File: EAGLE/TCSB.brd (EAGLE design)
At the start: 160 x 100 mm, 0 parts

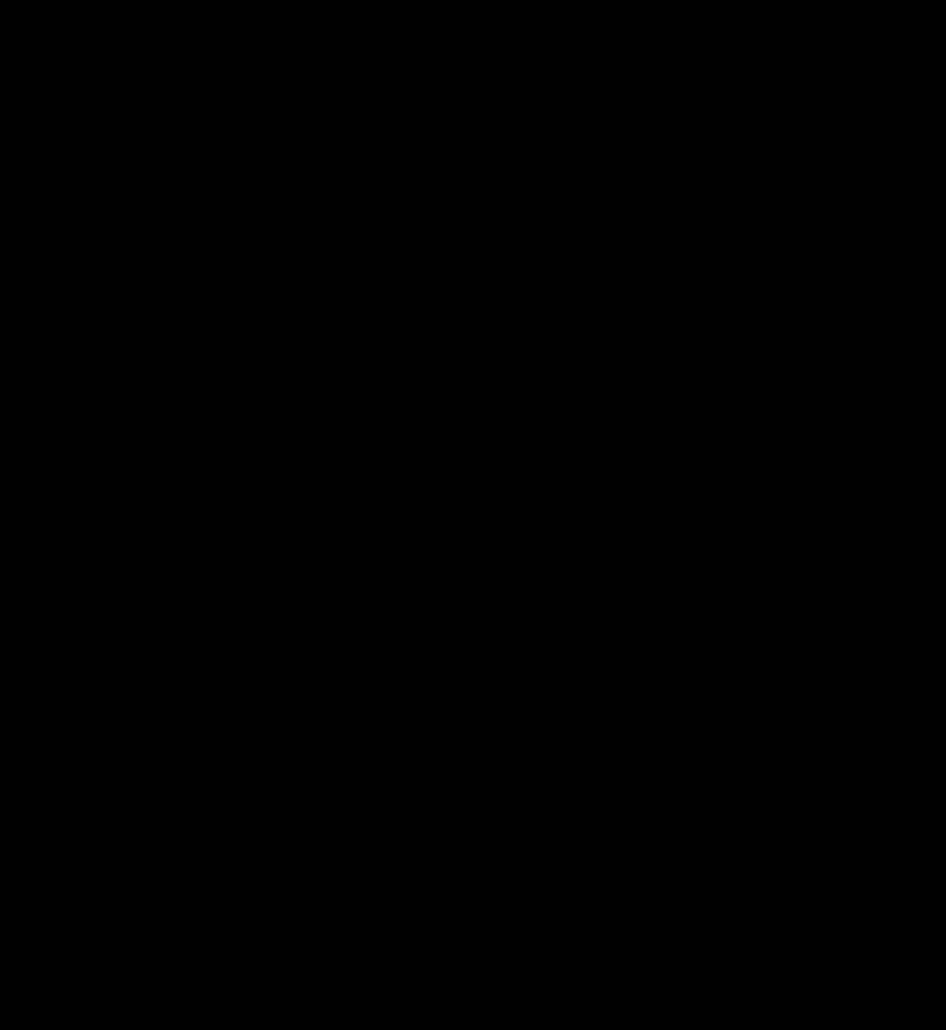
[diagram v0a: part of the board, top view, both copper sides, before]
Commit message: added board and firmware for two versions
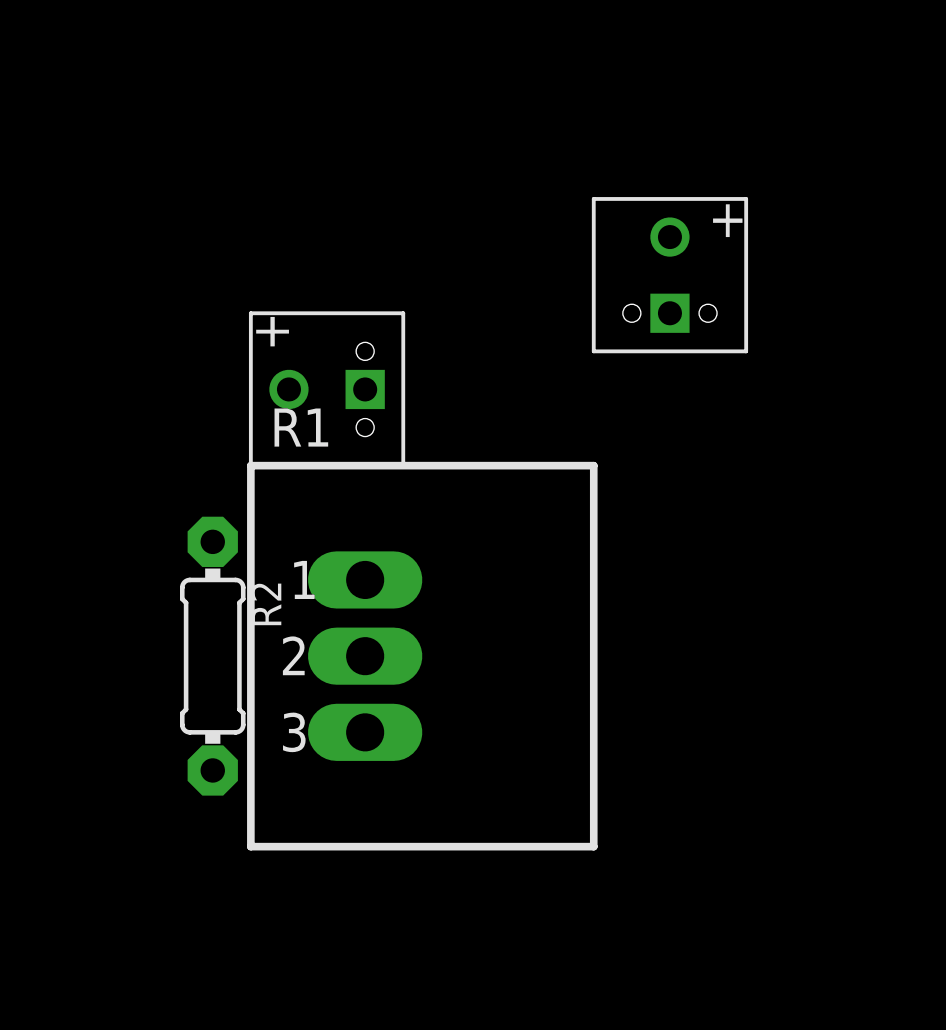
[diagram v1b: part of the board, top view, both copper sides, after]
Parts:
- added R1: (no value), bourns:308
- added R2: 10ohms, adafruit:0204/7
- added U$1, U$2: RCA-YELLOW, con-rca:RCA-YELLOW
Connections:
- new net N$1: R2.2, U$2.P$1
- new net N$2: R1.2, U$1.P$2, U$2.P$2
- new net N$3: R1.3, U$1.P$1
- new net N$4: R1.1, R2.1
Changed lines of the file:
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@@
 <layer number="48" name="Document" color="7" fill="1" visible="yes" active="yes"/>
 <layer number="49" name="Reference" color="7" fill="1" visible="yes" active="yes"/>
+<layer number="50" name="dxf" color="7" fill="1" visible="no" active="yes"/>
 <layer number="51" name="tDocu" color="7" fill="1" visible="yes" active="yes"/>
 <layer number="52" name="bDocu" color="7" fill="1" visible="yes" active="yes"/>
+<layer number="53" name="tGND_GNDA" color="7" fill="9" visible="no" active="no"/>
+<layer number="54" name="bGND_GNDA" color="1" fill="9" visible="no" active="no"/>
+<layer number="56" name="wert" color="7" fill="1" visible="yes" active="yes"/>
 <layer number="90" name="Modules" color="5" fill="1" visible="no" active="no"/>
 <layer number="91" name="Nets" color="2" fill="1" visible="no" active="no"/>
@@
 <layer number="97" name="Info" color="7" fill="1" visible="no" active="no"/>
 <layer number="98" name="Guide" color="6" fill="1" visible="no" active="no"/>
+<layer number="100" name="Muster" color="7" fill="1" visible="no" active="no"/>
+<layer number="101" name="Patch_Top" color="12" fill="4" visible="yes" active="yes"/>
+<layer number="102" name="Vscore" color="7" fill="1" visible="yes" active="yes"/>
+<layer number="104" name="Name" color="7" fill="1" visible="yes" active="yes"/>
+<layer number="116" name="Patch_BOT" color="9" fill="4" visible="yes" active="yes"/>
+<layer number="121" name="_tsilk" color="7" fill="1" visible="yes" active="yes"/>
+<layer number="122" name="_bsilk" color="7" fill="1" visible="yes" active="yes"/>
+<layer number="151" name="HeatSink" color="7" fill="1" visible="yes" active="yes"/>
+<layer number="200" name="200bmp" color="1" fill="10" visible="no" active="no"/>
+<layer number="201" name="201bmp" color="2" fill="1" visible="no" active="no"/>
+<layer number="202" name="202bmp" color="3" fill="1" visible="no" active="no"/>
+<layer number="203" name="203bmp" color="4" fill="10" visible="yes" active="yes"/>
+<layer number="204" name="204bmp" color="5" fill="10" visible="yes" active="yes"/>
+<layer number="205" name="205bmp" color="6" fill="10" visible="yes" active="yes"/>
+<layer number="206" name="206bmp" color="7" fill="10" visible="yes" active="yes"/>
+<layer number="207" name="207bmp" color="8" fill="10" visible="yes" active="yes"/>
+<layer number="208" name="208bmp" color="9" fill="10" visible="yes" active="yes"/>
+<layer number="250" name="Descript" color="7" fill="1" visible="no" active="no"/>
+<layer number="251" name="SMDround" color="7" fill="1" visible="no" active="no"/>
+<layer number="254" name="cooling" color="7" fill="1" visible="yes" active="yes"/>
 </layers>
 <board>
@@
 </autorouter>
 <elements>
+<element name="U$1" library="con-rca" package="RCA-YELLOW" value="RCA-YELLOW" x="33.02" y="25.4"/>
+<element name="U$2" library="con-rca" package="RCA-YELLOW" value="RCA-YELLOW" x="24.13" y="21.59" rot="R90"/>
+<element name="R1" library="bourns" package="308" value="" x="24.13" y="13.97"/>
+<element name="R2" library="adafruit" package="0204/7" value="10ohms" x="19.05" y="13.97" rot="R270"/>
 </elements>
 <signals>
+<signal name="N$1">
+<contactref element="U$2" pad="P$1"/>
+<contactref element="R2" pad="2"/>
+<wire x1="24.13" y1="22.86" x2="19.05" y2="10.16" width="0" layer="19" extent="1-1"/>
+</signal>
+<signal name="N$2">
+<contactref element="U$1" pad="P$2"/>
+<contactref element="R1" pad="2"/>
+<contactref element="U$2" pad="P$2"/>
+<wire x1="21.59" y1="22.86" x2="24.13" y2="13.97" width="0" layer="19" extent="1-1"/>
+<wire x1="34.29" y1="27.94" x2="21.59" y2="22.86" width="0" layer="19" extent="1-1"/>
+</signal>
+<signal name="N$3">
+<contactref element="U$1" pad="P$1"/>
+<contactref element="R1" pad="3"/>
+<wire x1="34.29" y1="25.4" x2="24.13" y2="11.43" width="0" layer="19" extent="1-1"/>
+</signal>
+<signal name="N$4">
+<contactref element="R1" pad="1"/>
+<contactref element="R2" pad="1"/>
+<wire x1="24.13" y1="16.51" x2="19.05" y2="17.78" width="0" layer="19" extent="1-1"/>
+</signal>
 </signals>
 </board>
